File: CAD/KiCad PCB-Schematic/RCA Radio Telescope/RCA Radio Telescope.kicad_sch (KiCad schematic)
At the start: 16 parts, among them J1 5V In For Filter Board, J2 5V From PoE Splitter, J3 3V Out For LNA, J4 5V Out For Filter Board, J5 Input from SDR, J6 USB_B_MICRO, U1 ZX60-P33ULN+, U2 ADALM Pluto SDR

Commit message: Updated PowerDataDistribute schematicto v1.4
- Added components for fuses and PMOS
- Created PCB v1.0
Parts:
- J2, J3, J4: footprint (none) -> Library:CONN_1729128_PXC
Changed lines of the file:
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@@
 		(exclude_from_sim no)
 		(in_bom yes)
-		(on_board yes)
+		(on_board no)
 		(dnp no)
 		(property "Reference" "U2"
@@
 			)
 		)
-		(property "Footprint" ""
+		(property "Footprint" "Library:CONN_1729128_PXC"
 			(at 175.26 116.84 0)
 			(effects
@@
 		(exclude_from_sim no)
 		(in_bom yes)
-		(on_board yes)
+		(on_board no)
 		(dnp no)
 		(property "Reference" "U9"
@@
 			)
 		)
-		(property "Footprint" ""
+		(property "Footprint" "Library:CONN_1729128_PXC"
 			(at 241.3 99.06 0)
 			(effects
@@
 		(exclude_from_sim no)
 		(in_bom yes)
-		(on_board yes)
+		(on_board no)
 		(dnp no)
 		(property "Reference" "U1"
@@
 			)
 		)
-		(property "Footprint" ""
+		(property "Footprint" "Library:CONN_1729128_PXC"
 			(at 255.27 113.03 0)
 			(effects
@@
 		(exclude_from_sim no)
 		(in_bom yes)
-		(on_board yes)
+		(on_board no)
 		(dnp no)
 		(fields_autoplaced yes)
@@
 		(exclude_from_sim no)
 		(in_bom yes)
-		(on_board yes)
+		(on_board no)
 		(dnp no)
 		(property "Reference" "F1"
@@
 		(exclude_from_sim no)
 		(in_bom yes)
-		(on_board yes)
+		(on_board no)
 		(dnp no)
 		(property "Reference" "J6"
@@
 		(exclude_from_sim no)
 		(in_bom yes)
-		(on_board yes)
+		(on_board no)
 		(dnp no)
 		(property "Reference" "U12"
@@
 		(exclude_from_sim no)
 		(in_bom yes)
-		(on_board yes)
+		(on_board no)
 		(dnp no)
 		(property "Reference" "U10"
@@
 		(exclude_from_sim no)
 		(in_bom yes)
-		(on_board yes)
+		(on_board no)
 		(dnp no)
 		(property "Reference" "U8"
@@
 		(exclude_from_sim no)
 		(in_bom yes)
-		(on_board yes)
+		(on_board no)
 		(dnp no)
 		(property "Reference" "U11"

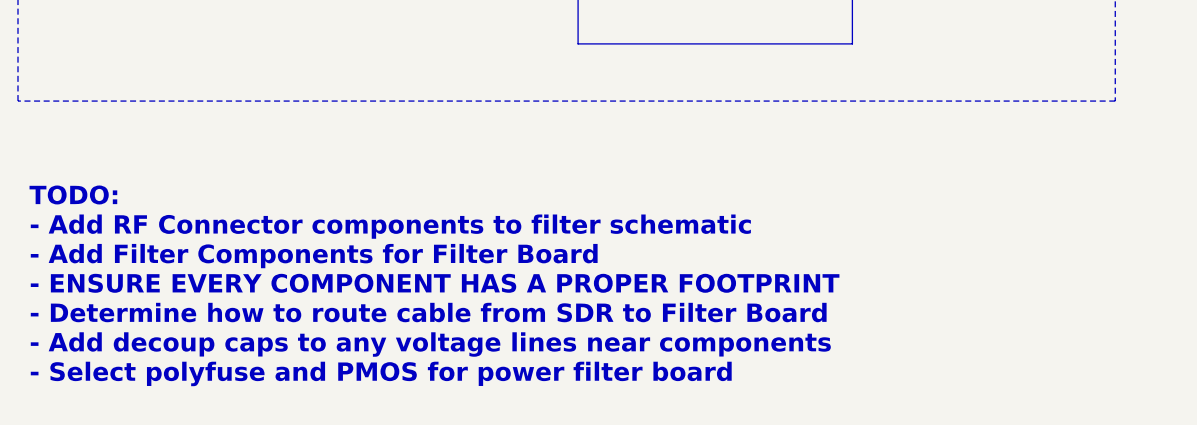
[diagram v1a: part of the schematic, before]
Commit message: Updated PowerData Board to v1.2
- Added zone fills for certain pins
- Added ground vias for mounting holes
- Minor readjustments to components
- Added silkscreen for voltage polarity
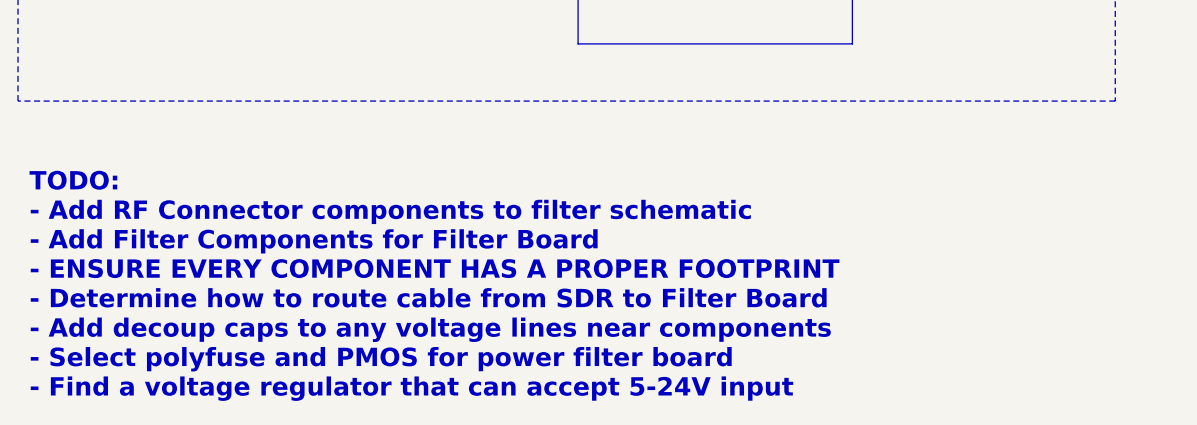
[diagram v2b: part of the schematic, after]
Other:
- note added: "TODO: - Add RF Connector components to filter schematic - Add Filter Components for Filter Board - ENSURE EVERY COMPONENT HAS A PROPER FOOTPRINT - Determine how to route cable from SDR to Filter Board - Add decoup caps to any voltage lines near components - Select polyfuse and PMOS for power filter board - Find a voltage regulator that can accept 5-24V input"
- note removed: "TODO: - Add RF Connector components to filter schematic - Add Filter Components for Filter Board - ENSURE EVERY COMPONENT HAS A PROPER FOOTPRINT - Determine how to route cable from SDR to Filter Board - Add decoup caps to any voltage lines near components - Select polyfuse and PMOS for power filter board"
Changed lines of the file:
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@@
 		)
 	)
-	(text "TODO:\n- Add RF Connector components to filter schematic\n- Add Filter Components for Filter Board\n- ENSURE EVERY COMPONENT HAS A PROPER FOOTPRINT\n- Determine how to route cable from SDR to Filter Board\n- Add decoup caps to any voltage lines near components\n- Select polyfuse and PMOS for power filter board"
+	(text "TODO:\n- Add RF Connector components to filter schematic\n- Add Filter Components for Filter Board\n- ENSURE EVERY COMPONENT HAS A PROPER FOOTPRINT\n- Determine how to route cable from SDR to Filter Board\n- Add decoup caps to any voltage lines near components\n- Select polyfuse and PMOS for power filter board\n- Find a voltage regulator that can accept 5-24V input"
 		(exclude_from_sim no)
 		(at 16.51 169.164 0)

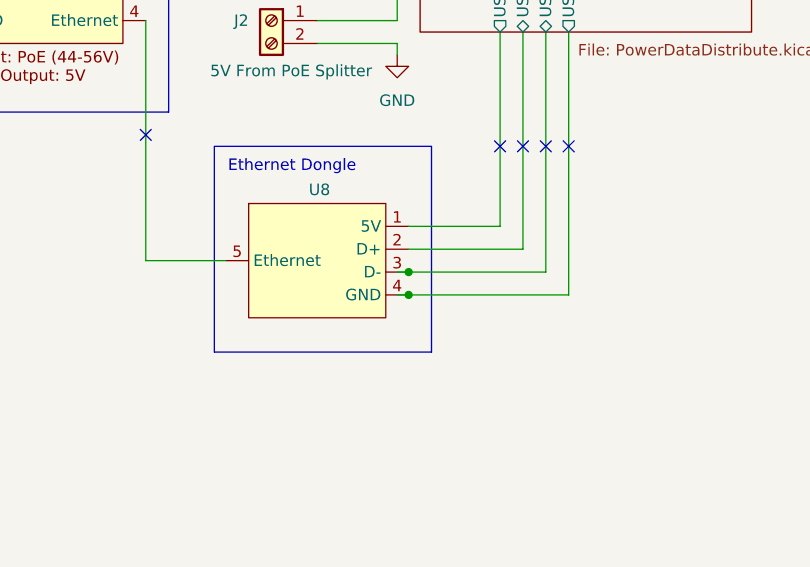
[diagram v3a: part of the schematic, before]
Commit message: Updated PowerData PCB to v1.6 and PowerData Schematic to v1.7
- Design Review with Andrew
- Fixed up various parts of PCB parameters
- May consider LDO or filtering for Power IC
- May want to consider a circuit breaker IC for LNA supply
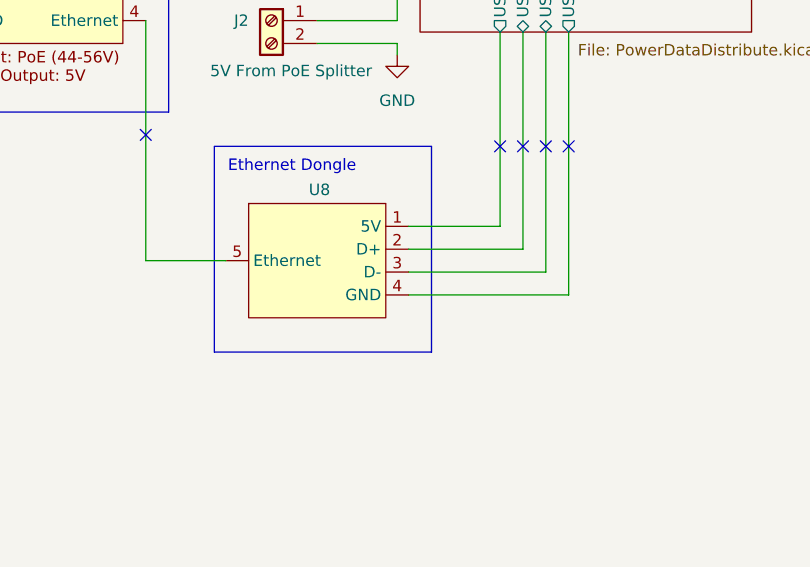
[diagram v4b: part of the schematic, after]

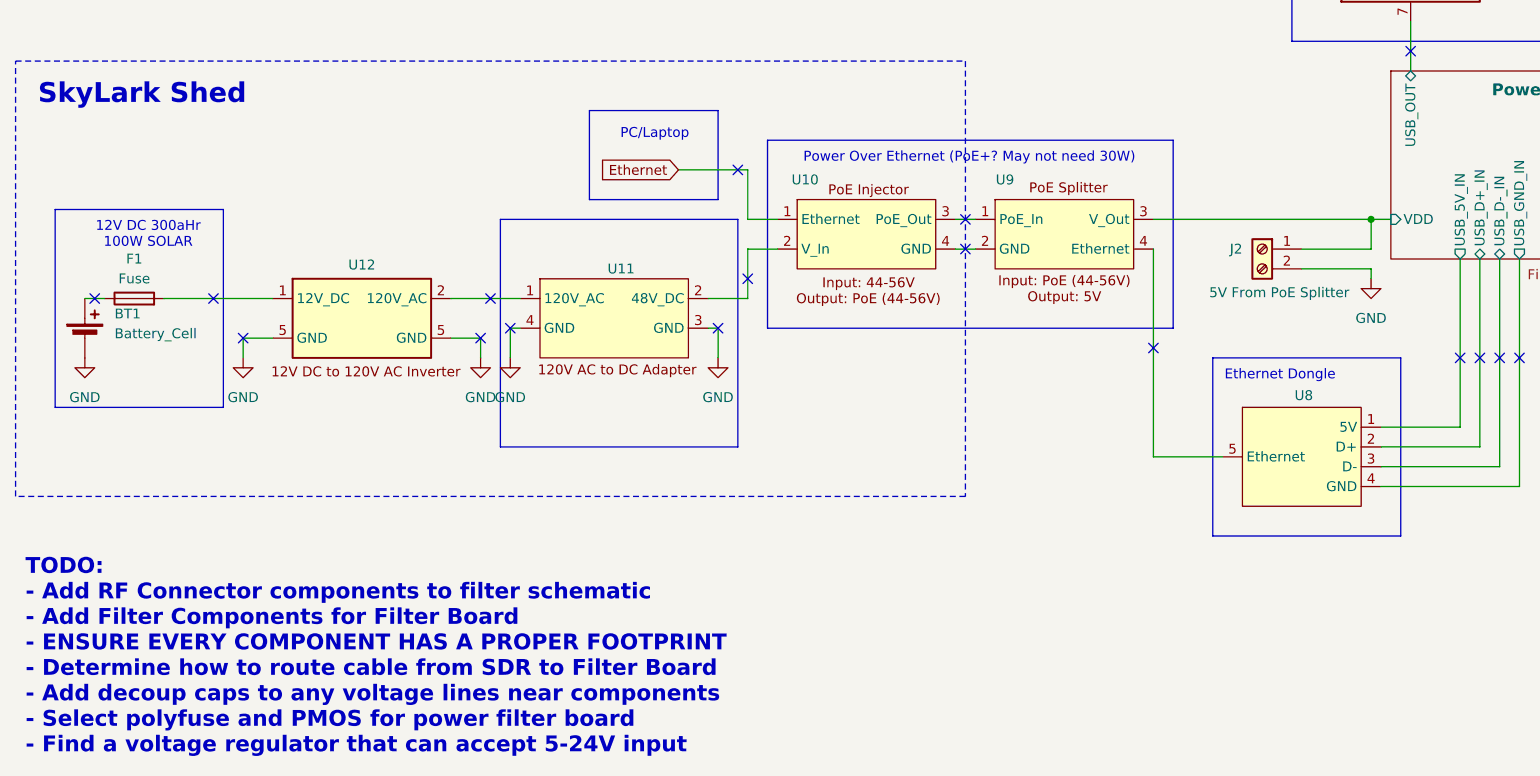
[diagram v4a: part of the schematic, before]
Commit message: Updated Root Schematic to v1.6 and P/D PCB to v2.2
- Changed input voltage to P/D board to 9-12V (Concerned about voltage drop of components which may not allow for 5V out)
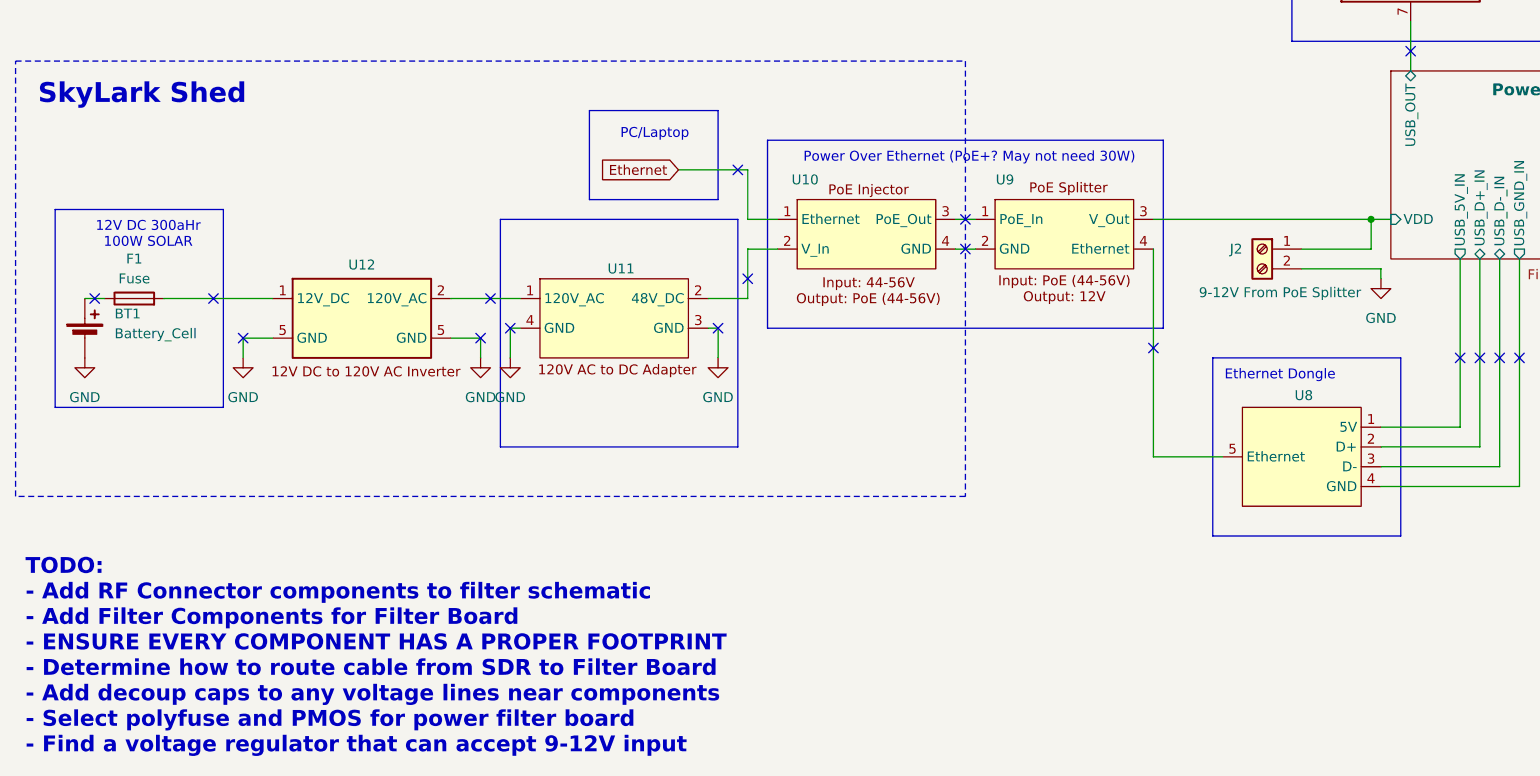
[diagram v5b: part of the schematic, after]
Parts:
- J2: value 5V From PoE Splitter -> 9-12V From PoE Splitter
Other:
- note added: "TODO: - Add RF Connector components to filter schematic - Add Filter Components for Filter Board - ENSURE EVERY COMPONENT HAS A PROPER FOOTPRINT - Determine how to route cable from SDR to Filter Board - Add decoup caps to any voltage lines near components - Select polyfuse and PMOS for power filter board - Find a voltage regulator that can accept 9-12V input"
- note removed: "TODO: - Add RF Connector components to filter schematic - Add Filter Components for Filter Board - ENSURE EVERY COMPONENT HAS A PROPER FOOTPRINT - Determine how to route cable from SDR to Filter Board - Add decoup caps to any voltage lines near components - Select polyfuse and PMOS for power filter board - Find a voltage regulator that can accept 5-24V input"
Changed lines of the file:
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@@
 	(title_block
 		(title "RCA Radio Telescope System")
-		(date "2025-02-09")
-		(rev "Version 1.5")
+		(date "2025-03-29")
+		(rev "Version 1.6")
 	)
 	(junction
@@
 	(wire
 		(pts
-			(xy 189.23 119.38) (xy 189.23 120.65)
+			(xy 190.5 119.38) (xy 190.5 120.65)
 		)
 		(stroke
@@
 	(wire
 		(pts
-			(xy 180.34 119.38) (xy 189.23 119.38)
+			(xy 180.34 119.38) (xy 190.5 119.38)
 		)
 		(stroke
@@
 	(rectangle
 		(start 111.76 102.87)
-		(end 163.83 127)
+		(end 162.56 127)
 		(stroke
 			(width 0)
@@
 		)
 	)
-	(text "TODO:\n- Add RF Connector components to filter schematic\n- Add Filter Components for Filter Board\n- ENSURE EVERY COMPONENT HAS A PROPER FOOTPRINT\n- Determine how to route cable from SDR to Filter Board\n- Add decoup caps to any voltage lines near components\n- Select polyfuse and PMOS for power filter board\n- Find a voltage regulator that can accept 5-24V input"
+	(text "TODO:\n- Add RF Connector components to filter schematic\n- Add Filter Components for Filter Board\n- ENSURE EVERY COMPONENT HAS A PROPER FOOTPRINT\n- Determine how to route cable from SDR to Filter Board\n- Add decoup caps to any voltage lines near components\n- Select polyfuse and PMOS for power filter board\n- Find a voltage regulator that can accept 9-12V input"
 		(exclude_from_sim no)
 		(at 16.51 169.164 0)
@@
 	(label "SDR_GPO_0"
 		(at 228.6 36.83 0)
+		(fields_autoplaced yes)
 		(effects
 			(font
@@
 	(label "SDR_GPO_GND"
 		(at 228.6 46.99 0)
+		(fields_autoplaced yes)
 		(effects
 			(font
@@
 	(label "SDR_GPO_1"
 		(at 228.6 39.37 0)
+		(fields_autoplaced yes)
 		(effects
 			(font
@@
 	(label "SDR_GPO_GND"
 		(at 71.12 60.96 0)
+		(fields_autoplaced yes)
 		(effects
 			(font
@@
 	(label "SDR_GPO_VDD"
 		(at 228.6 34.29 0)
+		(fields_autoplaced yes)
 		(effects
 			(font
@@
 	(label "SDR_GPO_1"
 		(at 86.36 55.88 180)
+		(fields_autoplaced yes)
 		(effects
 			(font
@@
 	(label "SDR_GPO_VDD"
 		(at 86.36 46.99 180)
+		(fields_autoplaced yes)
 		(effects
 			(font
@@
 	(label "SDR_GPO_0"
 		(at 86.36 52.07 180)
+		(fields_autoplaced yes)
 		(effects
 			(font
@@
 			)
 		)
-		(property "Value" "5V From PoE Splitter"
-			(at 186.436 122.428 0)
+		(property "Value" "9-12V From PoE Splitter"
+			(at 187.96 122.428 0)
 			(effects
 				(font
@@
 	(symbol
 		(lib_id "power:GND")
-		(at 189.23 120.65 0)
+		(at 190.5 120.65 0)
 		(unit 1)
 		(exclude_from_sim no)
@@
 		(fields_autoplaced yes)
 		(property "Reference" "#PWR032"
-			(at 189.23 127 0)
+			(at 190.5 127 0)
 			(effects
 				(font
@@
 		)
 		(property "Value" "GND"
-			(at 189.23 125.73 0)
+			(at 190.5 125.73 0)
 			(effects
 				(font
@@
 		)
 		(property "Footprint" ""
-			(at 189.23 120.65 0)
+			(at 190.5 120.65 0)
 			(effects
 				(font
@@
 		)
 		(property "Datasheet" ""
-			(at 189.23 120.65 0)
+			(at 190.5 120.65 0)
 			(effects
 				(font
@@
 		)
 		(property "Description" "Power symbol creates a global label with name \"GND\" , ground"
-			(at 189.23 120.65 0)
-			(effects
-				(font
+			(at 190.5 120.65 0)
+			(effects
+				(font
